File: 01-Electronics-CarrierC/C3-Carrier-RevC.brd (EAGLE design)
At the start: 32 x 82 mm, 56 parts, among them J1 18650 CELL, J2 LEFT MOTOR, J3 RIGHT MOTOR, J4 RUN SWITCH, J5 USB4125-GF-A-0190, Q1 FS8205A (Fortune TSSOP8), U1 ESP32-C3 SuperMini, U2 TC1508A, U3 TP4056-42-ESOP8, U4 DW01A-G, U5 MT3608, U6 TXU0104PWR

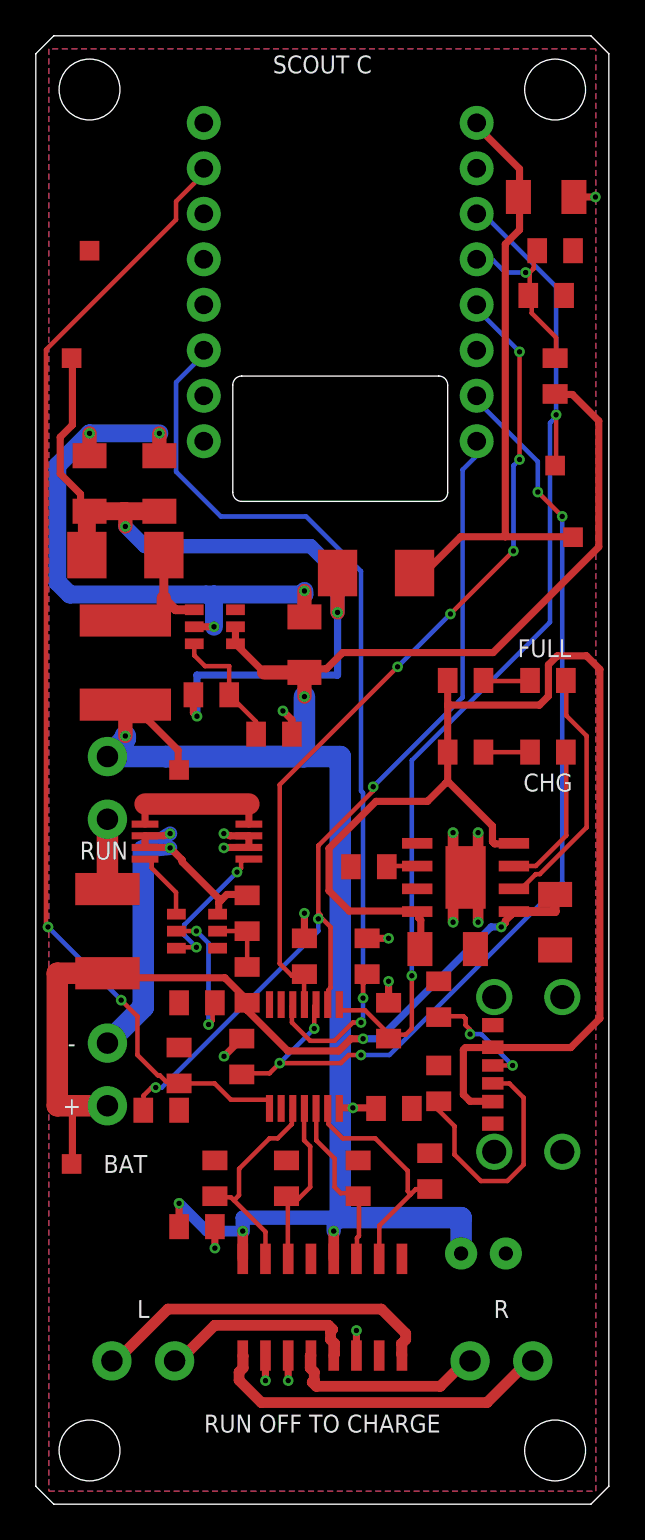
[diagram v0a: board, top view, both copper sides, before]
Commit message: Sync current Scout guide, firmware, Faces and v8 cases
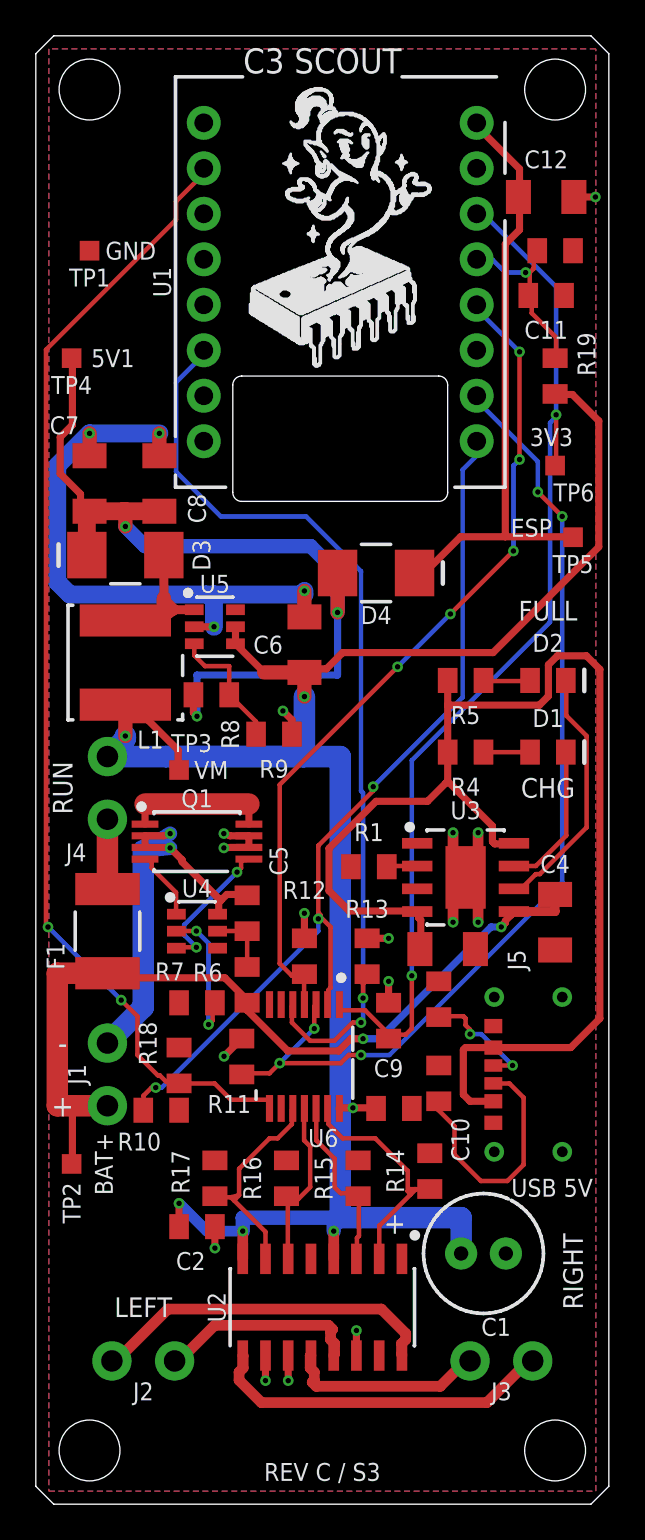
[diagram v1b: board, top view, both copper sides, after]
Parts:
- C1: value 100uF / 25V -> 100uF / 25V (FM)
- J5: value USB4125-GF-A-0190 -> TYPE-C 6P (SHOU HAN); device C3_SCOUT_REVC:USB4125-ROUND-STAKE -> C3_SCOUT_REVC:USB-C-SHOUHAN-6P-C456012
- Q1: value FS8205A (Fortune TSSOP8) -> 8205A (TECH PUBLIC)
- U4: value DW01A-G -> DW01A (PUOLOP)
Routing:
- net SW: track 7.62 -> 8.42 mm
- net INA: track 13.3 -> 13.8 mm
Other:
- board text added: "3V3"
- board text added: "5V1"
- board text added: "BAT+"
- board text added: "C3 SCOUT"
- board text added: "ESP"
- board text added: "ESP32-C3"
- board text added: "GND"
- board text added: "LEFT"
- board text added: "REV C"
- board text added: "REV C / S3"
- board text added: "RIGHT"
- board text added: "SCOUT"
- board text added: "SILK 03"
- board text added: "TEST POINTS"
- board text added: "TP1 GND"
- board text added: "TP2 BAT+"
- board text added: "TP3 MOTOR"
- board text added: "TP4 BOOST"
- board text added: "TP5 ESP5V"
- board text added: "TP6 3V3"
- board text added: "USB 5V"
- board text added: "USB END"
- board text added: "VM"
- board text removed: "BAT"
- board text removed: "C1"
- board text removed: "C10"
- board text removed: "C11"
- board text removed: "C12"
- board text removed: "C2"
- board text removed: "C4"
- board text removed: "C5"
- board text removed: "C6"
- board text removed: "C7"
- board text removed: "C8"
- board text removed: "C9"
- board text removed: "D1"
- board text removed: "D2"
- board text removed: "D3"
- board text removed: "D4"
- board text removed: "F1"
- board text removed: "J1"
- board text removed: "J2"
- board text removed: "J3"
- board text removed: "J4"
- board text removed: "J5"
- board text removed: "L"
- board text removed: "L1"
- board text removed: "Q1"
- board text removed: "R"
- board text removed: "R1"
- board text removed: "R10"
- board text removed: "R11"
- board text removed: "R12"
- board text removed: "R13"
- board text removed: "R14"
- board text removed: "R15"
- board text removed: "R16"
- board text removed: "R17"
- board text removed: "R18"
- board text removed: "R19"
- board text removed: "R2"
- board text removed: "R20"
- board text removed: "R3"
- board text removed: "R4"
- board text removed: "R5"
- board text removed: "R6"
- board text removed: "R7"
- board text removed: "R8"
- board text removed: "R9"
- board text removed: "RUN OFF TO CHARGE"
- board text removed: "SCOUT C"
- board text removed: "TP1"
- board text removed: "TP2"
- board text removed: "TP3"
- board text removed: "TP4"
- board text removed: "TP5"
- board text removed: "TP6"
- board text removed: "U1"
- board text removed: "U2"
- board text removed: "U3"
- board text removed: "U4"
- board text removed: "U5"
- board text removed: "U6"
